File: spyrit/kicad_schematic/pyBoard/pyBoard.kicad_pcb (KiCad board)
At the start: 2 copper layers, 83 parts, among them J1 USB_OTG, P1 CONN_01X02, SW1-RST1 SPST, SW2-USR1 SPST, U1 MCP1754ST-1802E/MB, U2 SPIRIT1, U3 STM32F405RGTx, U4 TPS22933, Y1 Crystal, Y2 8MHz

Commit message: [Derek] wiring intial commit
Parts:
- removed R16, R9]1: 4k7, Resistors_SMD:R_0805_HandSoldering
- removed R5: R, Resistors_SMD:R_0805_HandSoldering
- removed SW2-USR1: SPST, Buttons_Switches_SMD:SW_SPST_B3S-1100
- D5: footprint Diodes_SMD:DD-PAK_TO263_SingleDiode -> Diodes_SMD:SMB_Handsoldering
- P1: footprint Socket_Strips:Socket_Strip_Straight_1x02 -> Connect:PINHEAD1-3
- SW1-RST1: footprint Buttons_Switches_SMD:SW_SPST_B3S-1100 -> Buttons_Switches_SMD:SW_SPST_B3U-3000P-B
- Y1, Y2: footprint Oscillators:SI570_SI571_HandSoldering -> Crystals:Crystal_SMD_5032_2Pads
- moved J1 180.4 mm to (196.0, 72.8), turned to 180 degrees
- moved R13 126.9 mm to (179.4, 78.6), turned to 270 degrees
- moved R19 122.0 mm to (187.6, 86.1), turned to 180 degrees
- moved R6 118.1 mm to (176.0, 78.7), turned to 270 degrees
- moved R20 112.2 mm to (187.6, 83.6), turned to 180 degrees
- moved R18 111.3 mm to (187.6, 88.7), turned to 180 degrees
- moved R7 109.2 mm to (170.2, 78.7), turned to 270 degrees
- moved R8 108.0 mm to (167.6, 78.7), turned to 270 degrees
- moved L11 106.4 mm to (152.7, 105.7), turned to 90 degrees
- moved R9 104.9 mm to (165.1, 78.7), turned to 270 degrees
- moved R21 104.0 mm to (187.5, 81.1), turned to 180 degrees
- moved D3 101.7 mm to (167.6, 73.7), turned to 270 degrees
- moved R14 101.4 mm to (166.2, 107.1), turned to 270 degrees
- moved D1 99.2 mm to (176.0, 73.4), turned to 270 degrees
- moved U3 98.2 mm to (166.8, 93.8)
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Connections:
- C2 pad 1: RST# -> Net-(C2-Pad1)
- R1 pad 2: RST# -> Net-(C2-Pad1)
- SW1-RST1 pad 1: RST# -> Net-(C2-Pad1)
- U2 pad 10: GND -> Net-(C11-Pad1)
- U3 pad 58: PB6-SCL-X9 -> Net-(U3-Pad58)
- U3 pad 59: PB7-SDA-X10 -> Net-(U3-Pad59)
- U3 pad 7: RST# -> Net-(C2-Pad1)
- U4 pad 1: Net-(P1-Pad2) -> Net-(P1-Pad1)
- U4 pad 3: Net-(P1-Pad1) -> Net-(P1-Pad2)
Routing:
- net Net-(C16-Pad2): track 0.00 -> 39.0 mm
- net VBUS: track 0.00 -> 34.1 mm
- net PB10-LED_1: track 0.00 -> 30.8 mm
- net Net-(C4-Pad1): track 0.00 -> 25.7 mm
- net Net-(C14-Pad2): track 0.00 -> 25.5 mm
- net Net-(C8-Pad1): track 0.00 -> 23.0 mm
- net Net-(C15-Pad1): track 0.00 -> 20.7 mm
- net Net-(C10-Pad1): track 0.00 -> 19.5 mm
- net PB5-MMA_AVDD: track 0.00 -> 18.6 mm
- net PB11-LED_2: track 0.00 -> 17.7 mm
- net Net-(C2-Pad1): track 0.00 -> 17.5 mm
- net PC7-GPIO_2: track 0.00 -> 17.1 mm
- net PA12-DP: track 0.00 -> 17.1 mm
- net PB0-LED_3: track 0.00 -> 16.8 mm
- net PA11-DM: track 0.00 -> 16.2 mm
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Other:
- board outline added: 70.2 x 55.8 mm

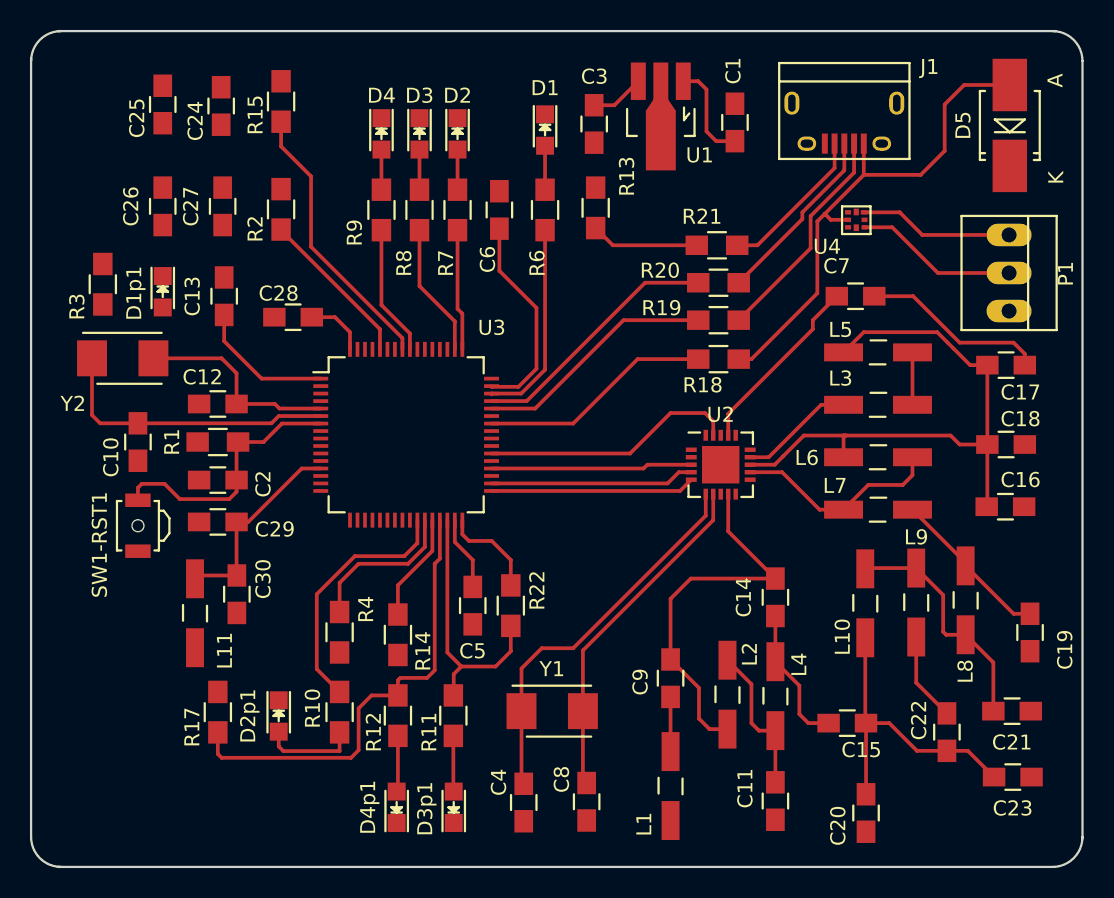
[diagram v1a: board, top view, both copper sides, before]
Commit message: [Derek] implementing 5/9 of pcb review improvements
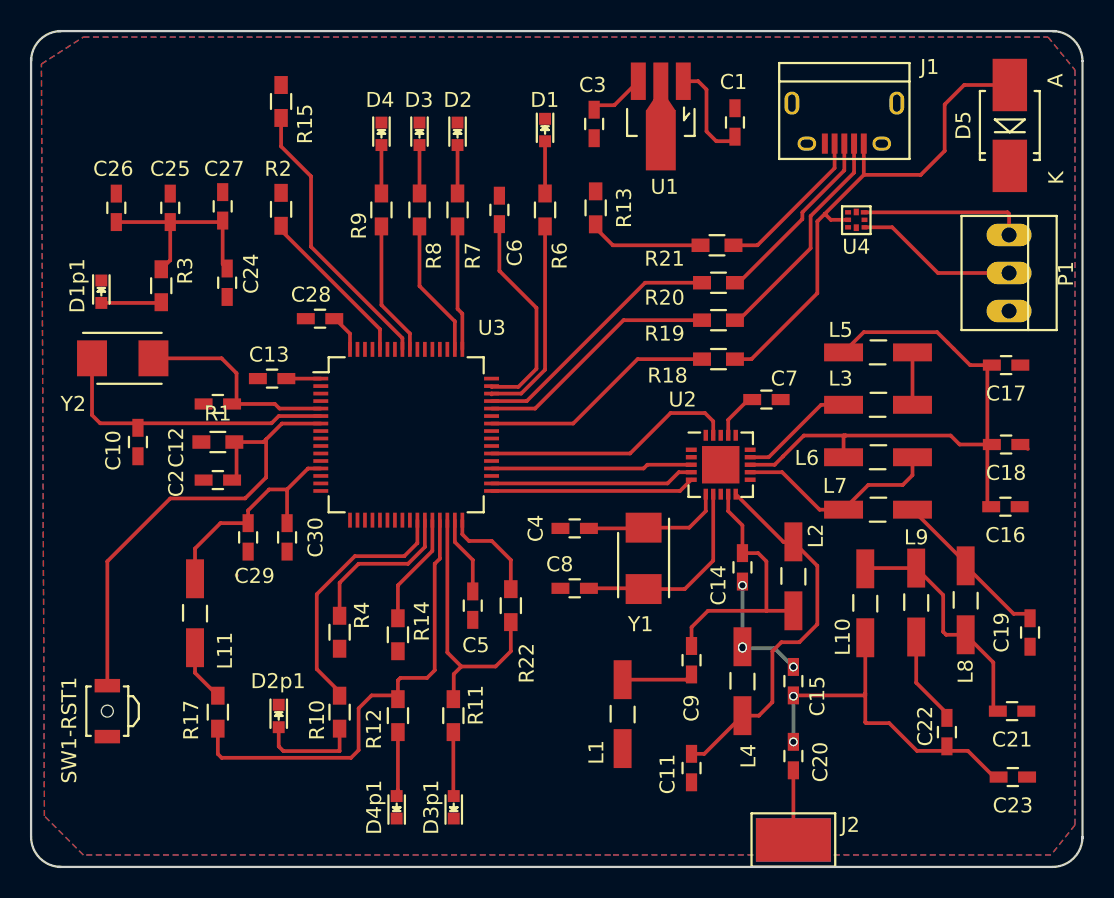
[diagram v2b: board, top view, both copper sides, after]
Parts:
- added J2: SMA, SMA, F.Cu at (192.6, 120.8)
- C1, C10, C11, C12, C13, C14, C15, C16, C17, C18, C19, C2, C20, C21, C22, C23, C24, C25, C26, C27, C28, C29, C3, C30, C4, C5, C6, C7, C8, C9: footprint Capacitors_SMD:C_0805_HandSoldering -> Capacitors_SMD:C_0603_HandSoldering
- D1, D1p1, D2, D2p1, D3, D3p1, D4, D4p1: footprint LEDs:LED_0805 -> LEDs:LED_0603
- R1, R10, R11, R12, R13, R14, R15, R17, R18, R19, R2, R20, R21, R22, R3, R4, R6, R7, R8, R9: footprint Resistors_SMD:R_0805_HandSoldering -> Resistors_SMD:R_0603_HandSoldering
- moved C4 18.6 mm to (178.0, 100.0), turned to 180 degrees
- moved C8 14.3 mm to (178.0, 104.0), turned to 180 degrees
- moved SW1-RST1 12.5 mm to (146.8, 112.2)
- moved Y1 11.9 mm to (182.6, 102.0), turned to 270 degrees
- moved C24 11.8 mm to (154.8, 83.6), turned to 270 degrees
- moved C7 9.11 mm to (190.8, 91.4)
- moved L2 9.04 mm to (192.6, 103.2)
- moved C25 6.92 mm to (151.0, 78.6)
- moved C13 6.36 mm to (157.8, 90.0), turned to 180 degrees
- moved C20 6.16 mm to (192.6, 115.2)
- moved C11 6.02 mm to (185.8, 116.0)
- moved L1 5.77 mm to (181.2, 112.4)
- moved C30 5.06 mm to (158.8, 100.6)
- moved C15 4.56 mm to (192.6, 110.2), turned to 90 degrees
- moved D1p1 4.10 mm to (146.4, 84.2)
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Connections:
- C2 pad 1: Net-(C2-Pad1) -> RST#
- R1 pad 2: Net-(C2-Pad1) -> RST#
- SW1-RST1 pad 1: Net-(C2-Pad1) -> RST#
- U3 pad 7: Net-(C2-Pad1) -> RST#
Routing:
- net RST#: track 0.00 -> 32.4 mm
- net Net-(C2-Pad1): track 17.5 -> 0.00 mm
- net Net-(C4-Pad1): track 25.7 -> 9.41 mm
- net +3V3: track 14.3 -> 30.4 mm
- net Net-(C11-Pad1): track 10.1 -> 25.3 mm
- net GND: track 12.8 -> 0.42 mm
- net Net-(C8-Pad1): track 23.0 -> 13.5 mm
- net Net-(C7-Pad2): track 12.3 -> 3.19 mm
- net Net-(C14-Pad2): track 25.5 -> 18.0 mm
- net VBAT: track 9.24 -> 2.30 mm
- net Net-(C20-Pad1): track 0.00 -> 4.65 mm
- net Net-(D1p1-Pad2): track 0.00 -> 4.02 mm
- net Net-(C15-Pad1): track 20.7 -> 24.0 mm, vias 0 -> 2
- net A3V3: track 13.6 -> 15.7 mm
- net Net-(C9-Pad2): track 3.65 -> 4.74 mm
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- added copper zone on F.Cu, net +3V3
- added copper zone on B.Cu, net GND

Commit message: [Derek] creating multiple layered PCB board with (hopefully) valid 3V3 and GND layers and connections
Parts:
- moved C28 2.63 mm to (158.4, 86.4)
- moved C4 1.08 mm to (179.0, 100.4)
- moved C8 1.08 mm to (179.0, 104.4)
- moved Y1 0.89 mm to (183.4, 102.4)
- moved R2 0.50 mm to (158.0, 78.4)
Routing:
- net GND: track 0.42 -> 134.0 mm, vias 0 -> 34
- net RST#: track 32.4 -> 97.6 mm, vias 0 -> 2
- net PB1-SDN: track 10.4 -> 48.8 mm, vias 0 -> 2
- net LED_BLU: track 2.68 -> 37.8 mm, vias 0 -> 2
- net PB8-GPIO_1: track 0.00 -> 33.7 mm, vias 0 -> 2
- net VIN: track 6.75 -> 37.9 mm, vias 0 -> 3
- net +3V3: track 30.4 -> 61.3 mm, vias 0 -> 12
- net PB9-GPIO_0: track 0.00 -> 30.7 mm, vias 0 -> 2
- net PC6-GPIO_3: track 0.00 -> 20.4 mm, vias 0 -> 2
- net PA10-ID: track 7.23 -> 24.8 mm, vias 0 -> 2
- net PB14-MISO: track 0.00 -> 14.1 mm, vias 0 -> 2
- net Net-(C20-Pad1): track 4.65 -> 9.67 mm, vias 0 -> 1
- net PC7-GPIO_2: track 17.1 -> 20.0 mm
- net BOOT0-P1: track 10.7 -> 13.0 mm
- net Net-(C8-Pad1): track 13.5 -> 11.8 mm
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- added copper zone on In2.Cu, net +3V3
- added copper zone on In1.Cu, net GND
- removed copper zone on F.Cu, net +3V3
- removed copper zone on B.Cu, net GND
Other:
- outline, holes or cut-outs redrawn
- copper layers 2 -> 4

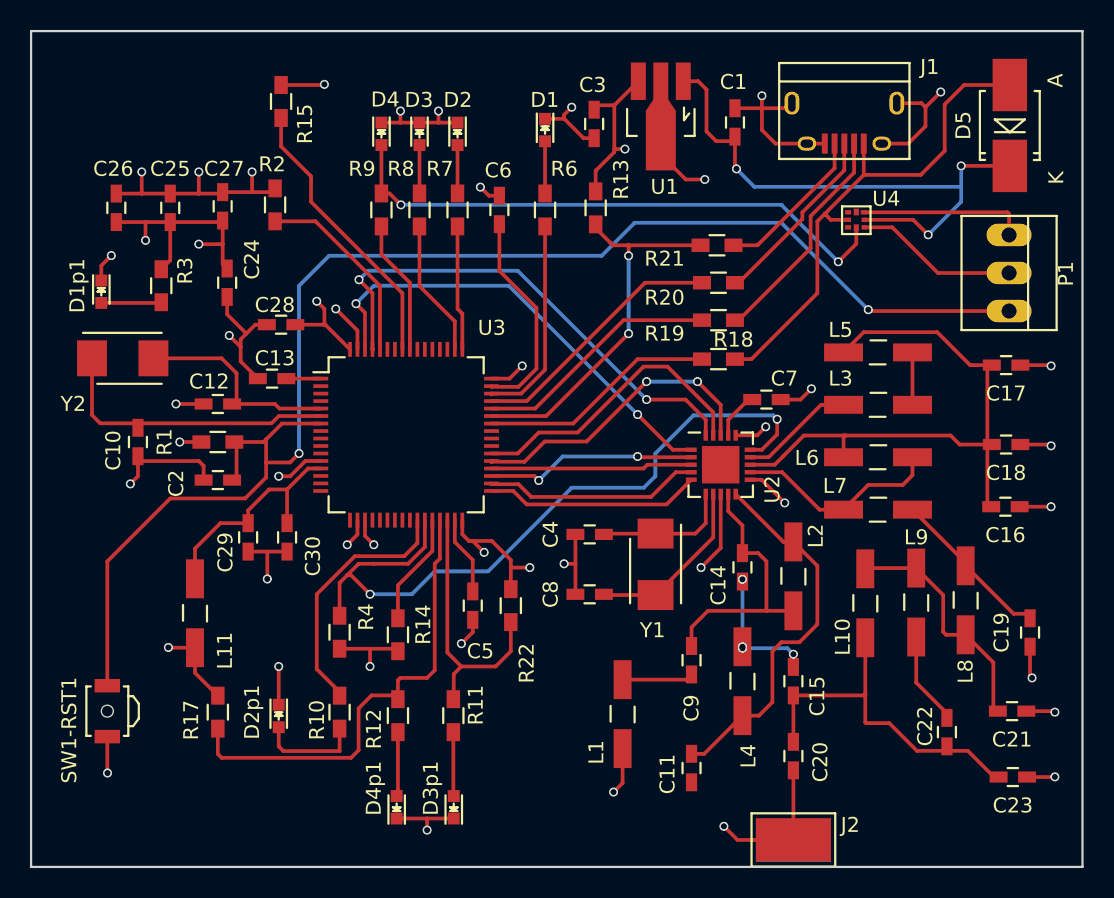
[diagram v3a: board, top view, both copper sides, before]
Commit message: Added Mounting holes
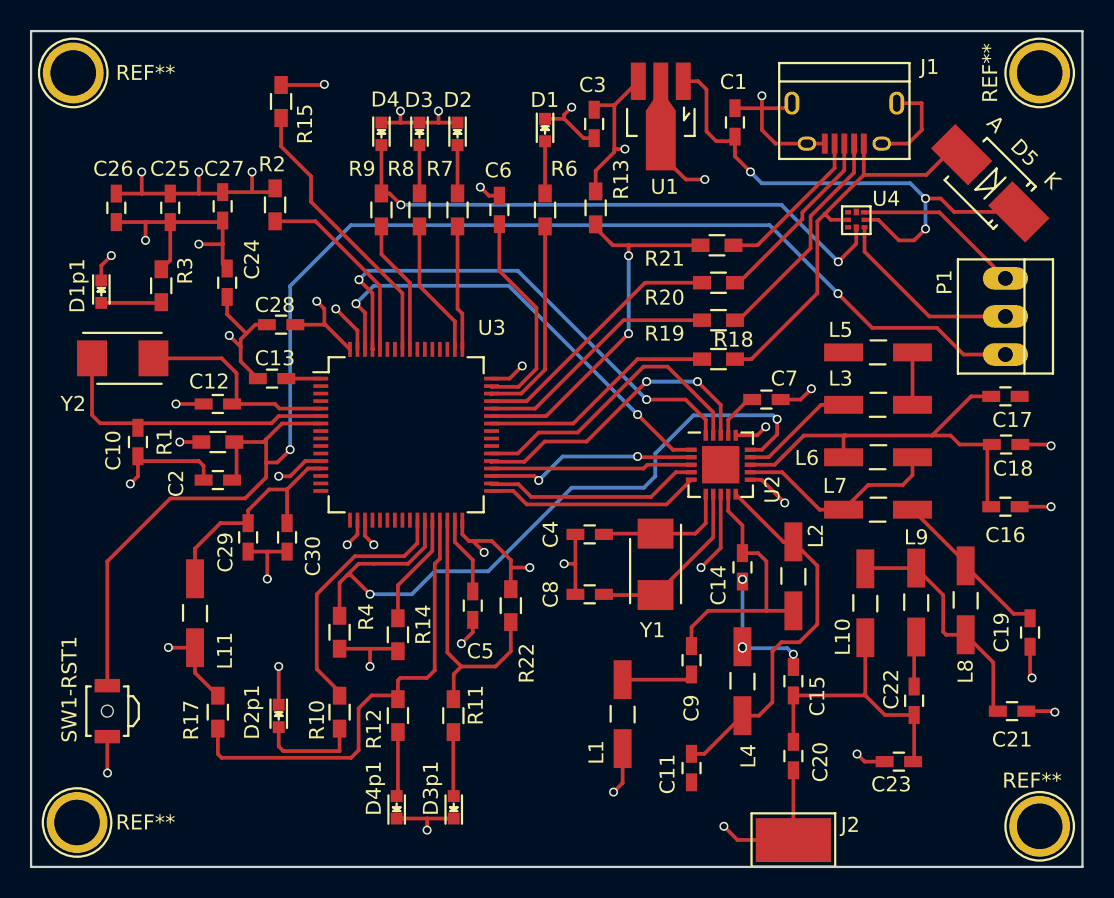
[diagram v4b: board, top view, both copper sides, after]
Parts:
- added REF**: 1pin, Connect:1pin, F.Cu at (144.8, 119.6)
- added REF**: 1pin, Connect:1pin, F.Cu at (144.5, 69.6)
- added REF**: 1pin, Connect:1pin, F.Cu at (209.0, 119.9)
- added REF**: 1pin, Connect:1pin, F.Cu at (209.0, 69.6)
- moved C23 7.68 mm to (199.6, 115.6), turned to 0 degrees
- moved D5 4.08 mm to (205.7, 77.0), turned to 135 degrees
- moved C22 3.03 mm to (200.7, 111.5)
- moved P1 2.91 mm to (206.8, 85.9)
- moved C17 2.09 mm to (206.8, 91.2)
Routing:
- net Net-(C16-Pad2): track 39.0 -> 27.7 mm
- net VBUS: track 34.1 -> 27.1 mm
- net Net-(C15-Pad1): track 24.0 -> 18.7 mm
- net GND: track 134.0 -> 130.4 mm, vias 34 -> 32
- net Net-(C22-Pad1): track 5.95 -> 3.36 mm
- net VIN: track 37.9 -> 35.5 mm
- net Net-(P1-Pad2): track 10.9 -> 12.8 mm
- net RST#: track 97.6 -> 98.3 mm

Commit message: Updated 3D diagram
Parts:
- renumbered REF** to REF1, REF** to REF2, REF** to REF3, REF** to REF4
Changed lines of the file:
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@@
     (descr "module 1 pin (ou trou mecanique de percage)")
     (tags DEV)
-    (fp_text reference REF** (at 4.572 0) (layer F.SilkS)
+    (fp_text reference REF2 (at 3.302 0 90) (layer F.SilkS)
       (effects (font (size 1 1) (thickness 0.15)))
     )
@@
     (descr "module 1 pin (ou trou mecanique de percage)")
     (tags DEV)
-    (fp_text reference REF** (at 4.826 0) (layer F.SilkS)
+    (fp_text reference REF1 (at 3.556 -0.254 90) (layer F.SilkS)
       (effects (font (size 1 1) (thickness 0.15)))
     )
@@
     (descr "module 1 pin (ou trou mecanique de percage)")
     (tags DEV)
-    (fp_text reference REF** (at -0.508 -3.048) (layer F.SilkS)
+    (fp_text reference REF3 (at -3.302 0 90) (layer F.SilkS)
       (effects (font (size 1 1) (thickness 0.15)))
     )
@@
     (descr "module 1 pin (ou trou mecanique de percage)")
     (tags DEV)
-    (fp_text reference REF** (at -3.302 0 90) (layer F.SilkS)
+    (fp_text reference REF4 (at -3.302 0 90) (layer F.SilkS)
       (effects (font (size 1 1) (thickness 0.15)))
     )
